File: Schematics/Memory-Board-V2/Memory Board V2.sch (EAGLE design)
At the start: 15 parts, among them IC4 27C128P, IC5 74HC174N, U1 GAL22V10D-DIP

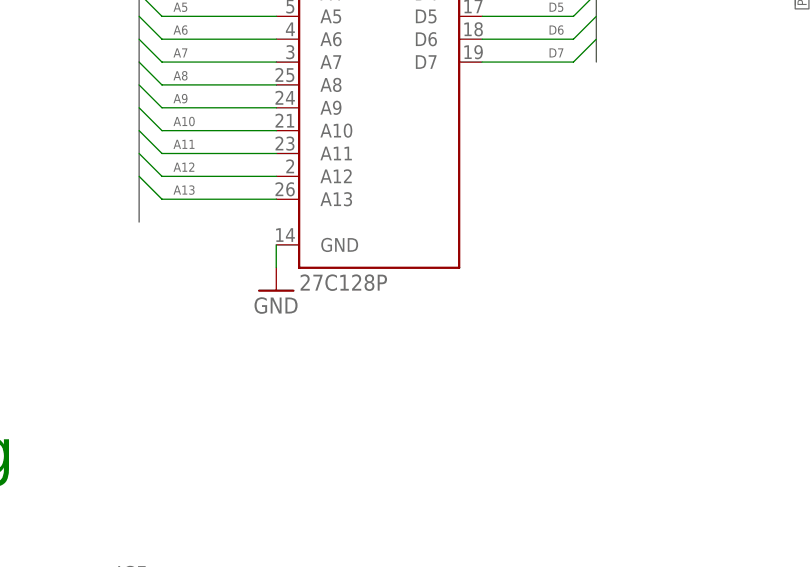
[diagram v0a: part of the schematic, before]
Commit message: Updated to have a formal Timer IRQ.  Currently this is T1 on the W65C22 on the GPIO card, so if you want to use it that card must be present.
The prebuilt ROM ToEVID.bin uses this card at 0xC040.

A couple of minor whoopsies have been fixed as well.
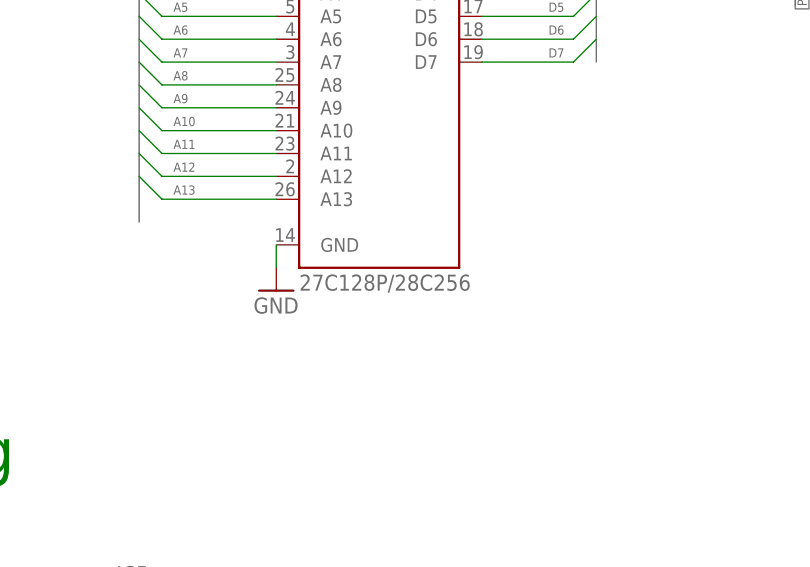
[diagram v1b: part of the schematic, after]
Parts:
- IC4: value 27C128P -> 27C128P/28C256
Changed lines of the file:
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@@
 <part name="GND3" library="supply1" deviceset="GND" device=""/>
 <part name="IC1" library="memory-hitachi" deviceset="62256P" device=""/>
-<part name="IC4" library="microchip" deviceset="27*128" device="P" technology="C"/>
+<part name="IC4" library="microchip" deviceset="27*128" device="P" technology="C" value="27C128P/28C256"/>
 <part name="IC2" library="memory-hitachi" deviceset="62256P" device=""/>
 <part name="IC3" library="memory-hitachi" deviceset="62256P" device=""/>
